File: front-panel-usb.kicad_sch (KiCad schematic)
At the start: 107 parts, among them J4 USB-C_Kycon_KUSBX-SL2-CS1N24-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, J5 Tag-Connect_TC2050-IDC-NL_2x5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, J6 USB-C_Kycon_KUSBX-SL2-CS1N24-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, J7 USB-C_Kycon_KUSBX-SL2-CS1N24-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, Q1 PJE138K, U11 TPD4E05U06QDQARQ1, U12 FT4232H_VQFN, U13 NCP718BSN330T1G, U14 74LVC06ABQ, U15 AP22615B_TSOT26, U16 AP22615B_TSOT26, U17 FUSB303B, U18 FUSB303B, U19 TPD4E05U06QDQARQ1, U20 TPD4E05U06QDQARQ1, Y3 Resonator_12MHz_ABM8G

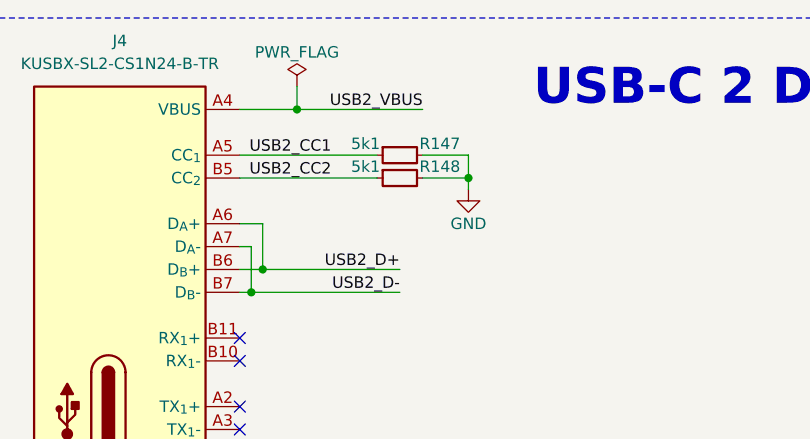
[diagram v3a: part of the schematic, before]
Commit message: [#83767] Replace 0201 resistors with 0402
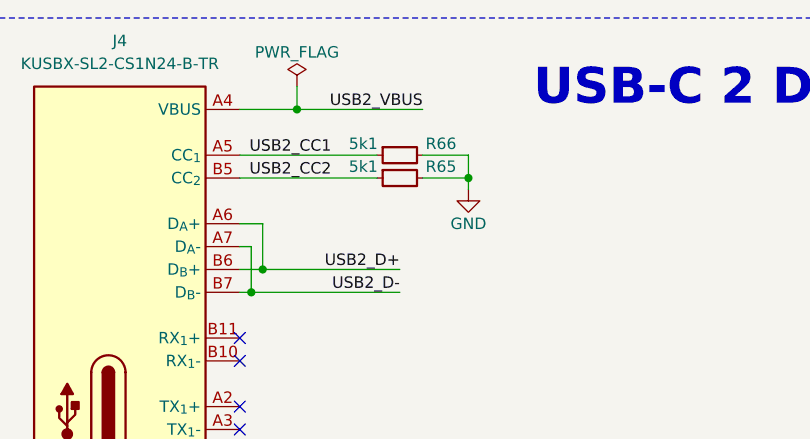
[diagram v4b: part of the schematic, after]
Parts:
- removed R147, R148: R_5k1_0201, antmicro-footprints:R_0201, symbol antmicroResistorsmisc:R_5k1_0201
- added R65, R66: R_5k1_0402, antmicro-footprints:R_0402_1005Metric, symbol antmicroResistors0402:R_5k1_0402
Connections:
- net GND: now also R65.2, R66.2
- net USB2_CC1: now also R66.1
- net USB2_CC2: now also R65.1

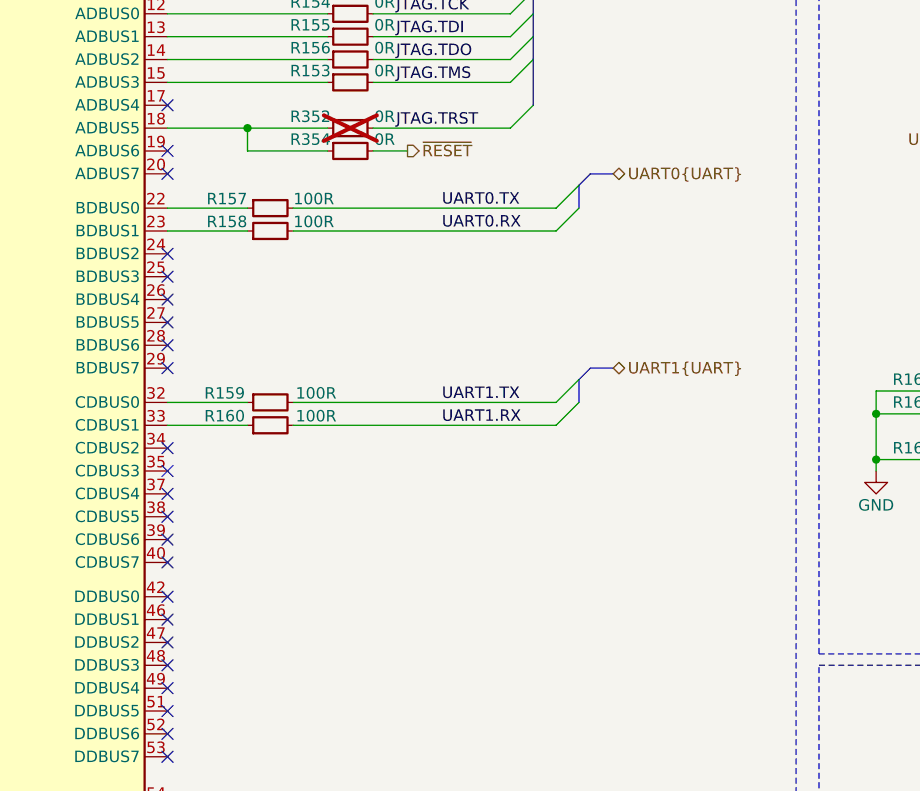
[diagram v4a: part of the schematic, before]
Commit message: [#83767] Move UART on FTDI from BDBUS
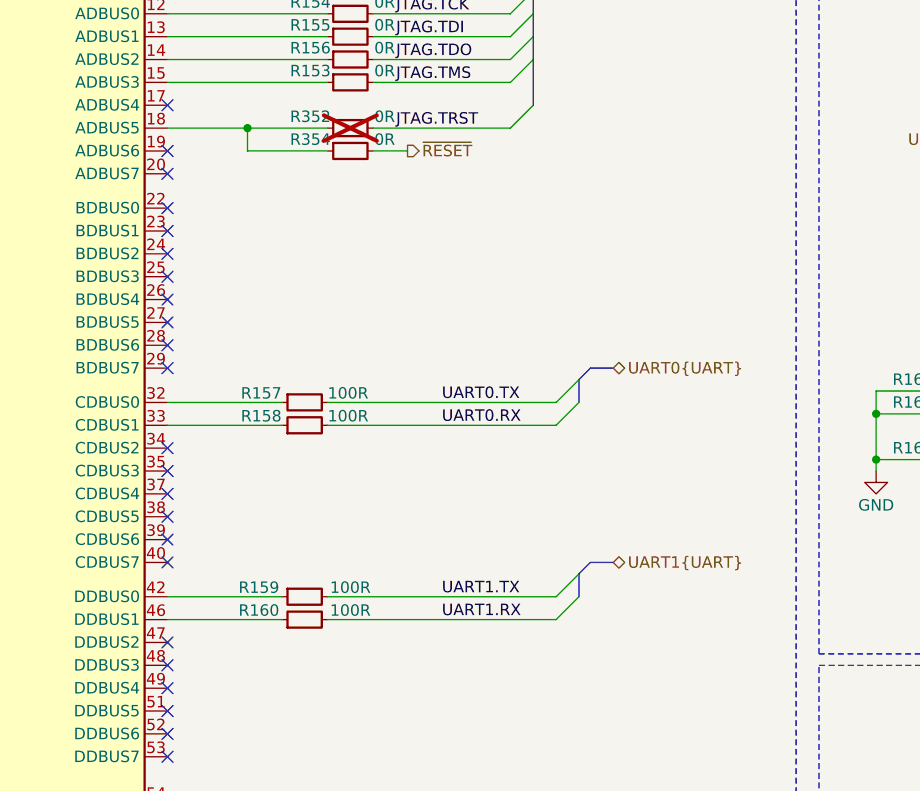
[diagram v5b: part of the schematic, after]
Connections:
- net at R158.1: now also U12.33 (CDBUS1); no longer U12.23 (BDBUS1)
- net at U12.22 (BDBUS0): no longer R157.1
- net at U12.32 (CDBUS0): now also R157.1; no longer R159.1
- net at R160.1: now also U12.46 (DDBUS1); no longer U12.33 (CDBUS1)
- net at U12.42 (DDBUS0): now also R159.1
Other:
- moved on the sheet: R157, R158, R159, R160

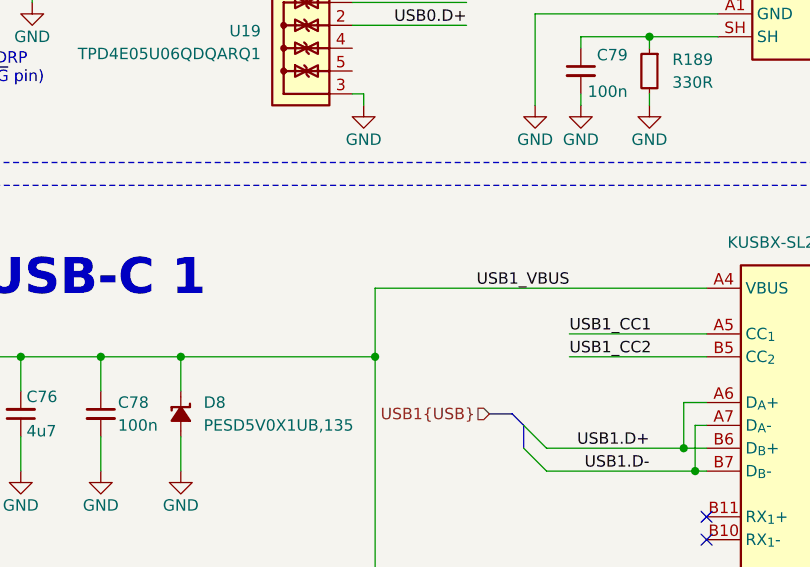
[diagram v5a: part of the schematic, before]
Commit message: [#84615] Connect Vbus detection to OSM
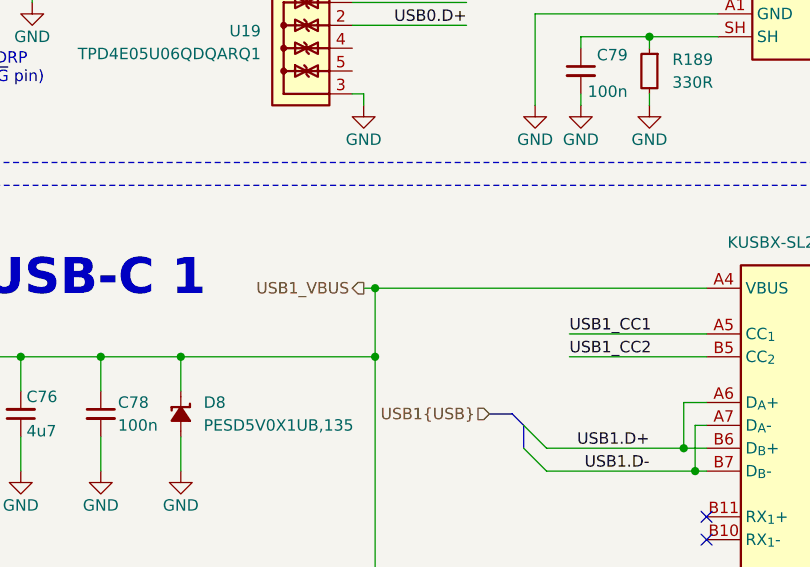
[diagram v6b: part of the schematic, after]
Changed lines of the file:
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@@
 	)
 	(junction
+		(at 337.82 118.11)
+		(diameter 0)
+		(color 0 0 0 0)
+	)
+	(junction
 		(at 287.02 135.89)
 		(diameter 0)
@@
 	(wire
 		(pts
+			(xy 336.55 118.11) (xy 337.82 118.11)
+		)
+		(stroke
+			(width 0)
+			(type default)
+		)
+	)
+	(wire
+		(pts
 			(xy 360.68 90.17) (xy 368.3 90.17)
 		)
@@
 		)
 	)
-	(label "USB1_VBUS"
-		(at 359.41 118.11 180)
-		(effects
-			(font
-				(size 1.27 1.27)
-			)
-			(justify right bottom)
-		)
-	)
 	(label "VCORE"
 		(at 85.09 144.78 0)
@@
 		)
 	)
+	(hierarchical_label "USB1_VBUS"
+		(shape output)
+		(at 336.55 118.11 180)
+		(effects
+			(font
+				(size 1.27 1.27)
+			)
+			(justify right)
+		)
+	)

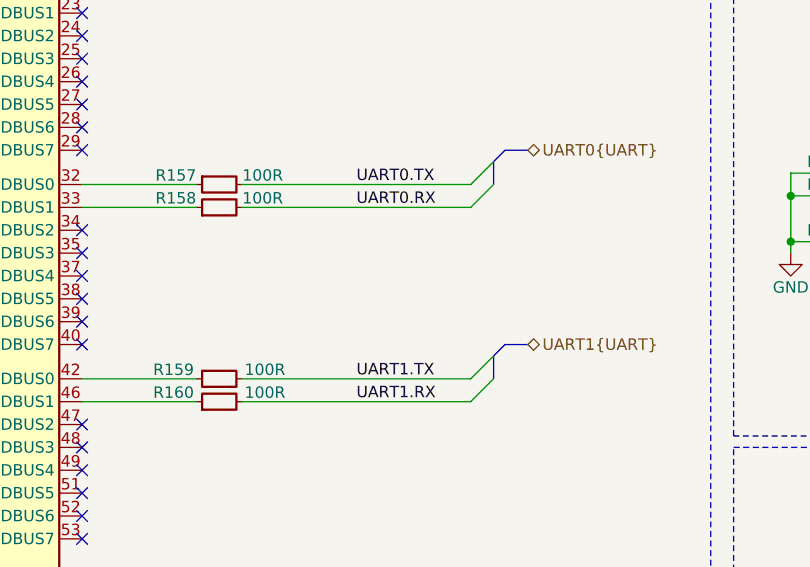
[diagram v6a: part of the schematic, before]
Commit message: [#84768] Add missing connections on sch
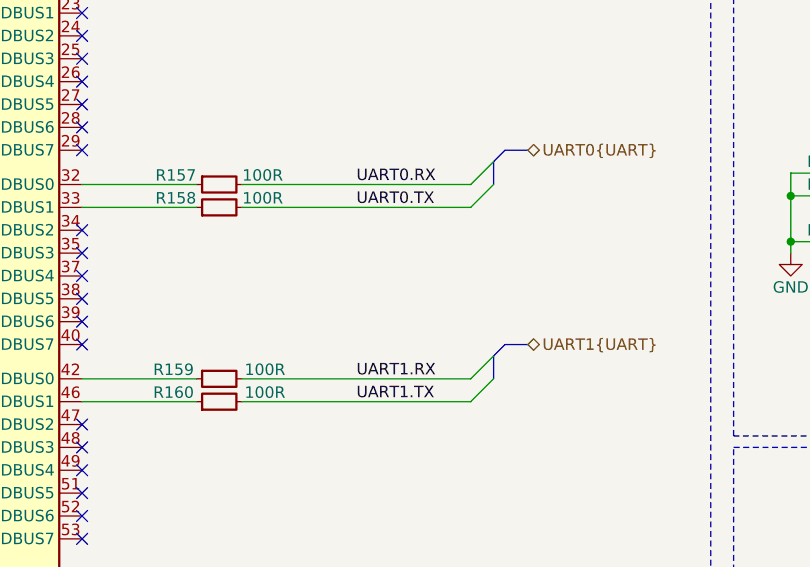
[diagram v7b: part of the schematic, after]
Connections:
- net UART0.RX: now also R157.2; no longer R158.2
- net UART0.TX: now also R158.2; no longer R157.2
- net UART1.RX: now also R159.2; no longer R160.2
- net UART1.TX: now also R160.2; no longer R159.2
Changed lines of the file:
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@@
 	)
 	(label "UART1.RX"
-		(at 171.45 196.85 0)
+		(at 171.45 194.31 0)
 		(effects
 			(font
@@
 	)
 	(label "UART0.TX"
-		(at 171.45 172.72 0)
+		(at 171.45 175.26 0)
 		(effects
 			(font
@@
 	)
 	(label "UART1.TX"
-		(at 171.45 194.31 0)
+		(at 171.45 196.85 0)
 		(effects
 			(font
@@
 	)
 	(label "UART0.RX"
-		(at 171.45 175.26 0)
-		(effects
-			(font
+		(at 171.45 172.72 0)
+		(effects
+			(font
